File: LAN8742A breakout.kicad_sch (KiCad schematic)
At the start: 35 parts, among them J1 HR911105A_C12074, J2 J_RMII, J3 J_POW, SW1 nRST_SW, U1 LAN8720A, Y1 25MHz

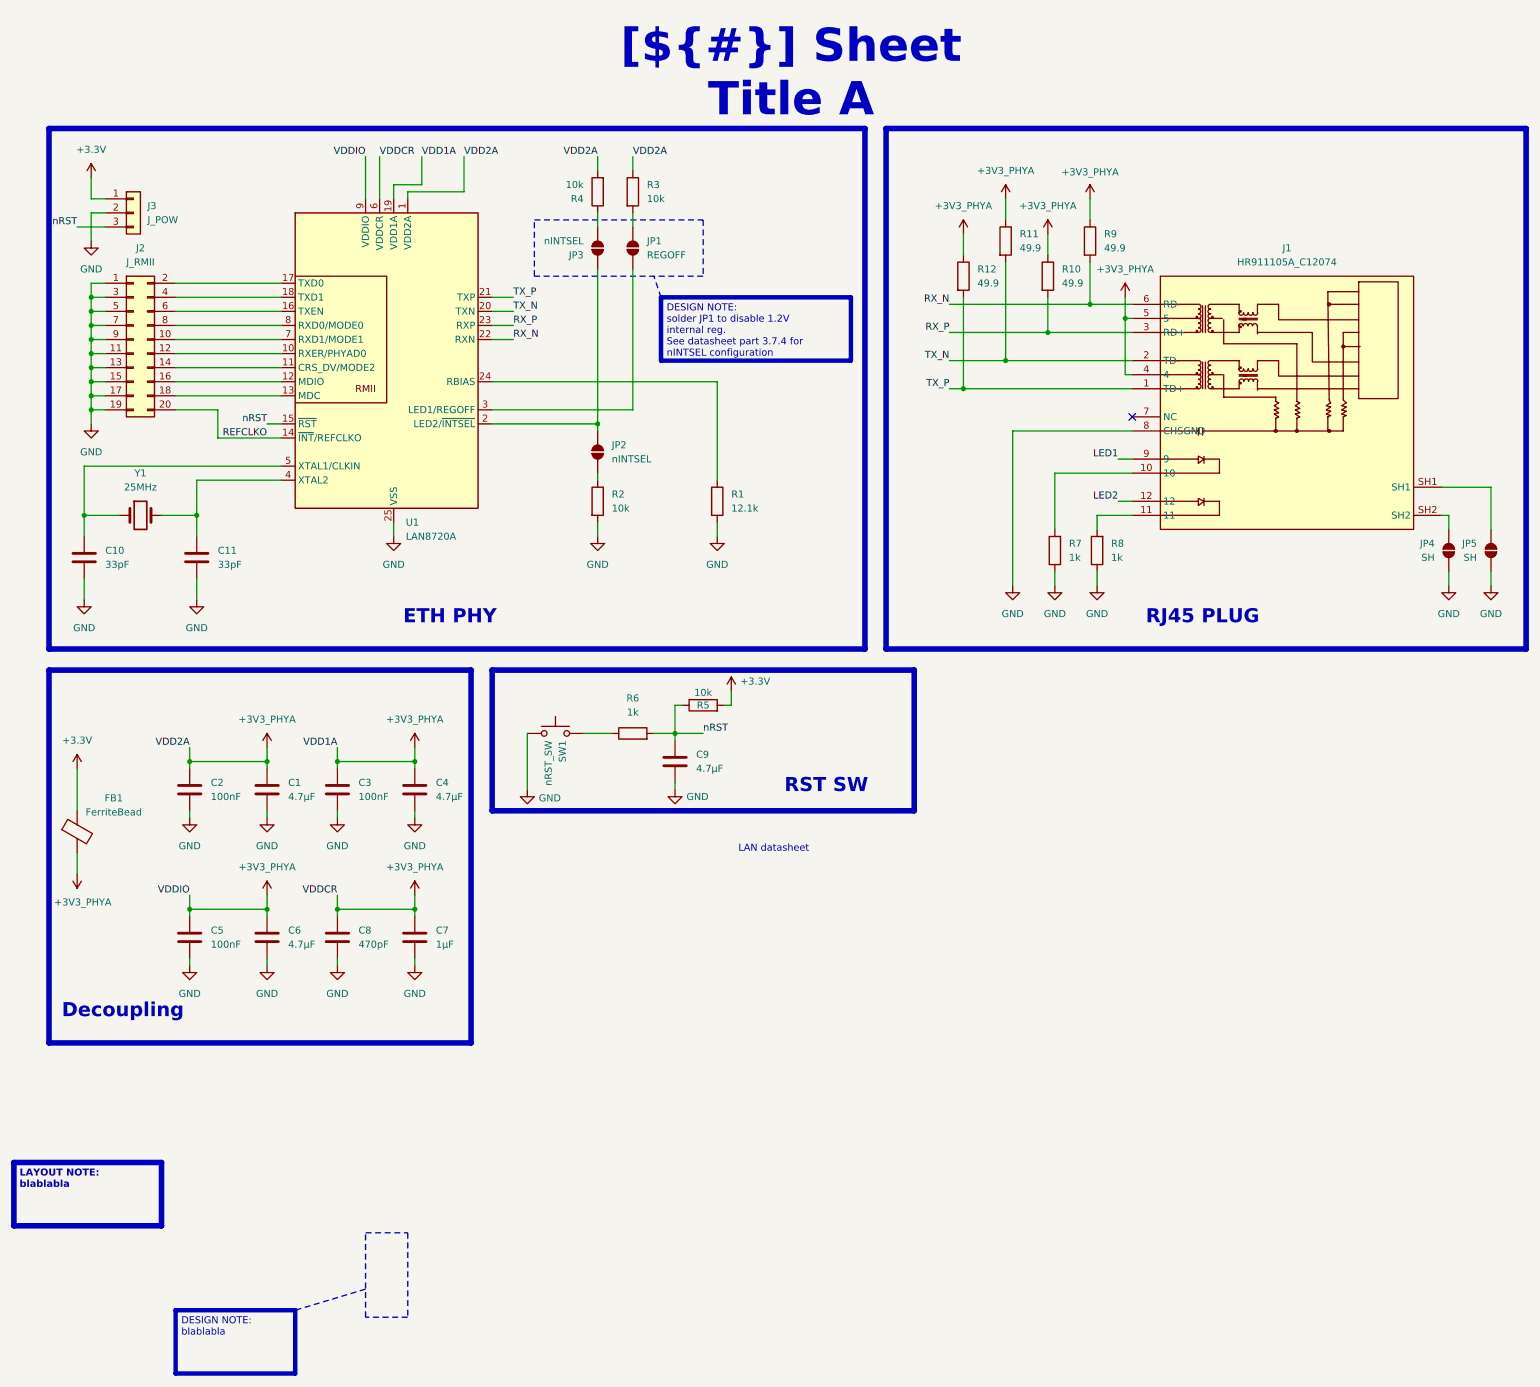
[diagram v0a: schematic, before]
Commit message: routed signals
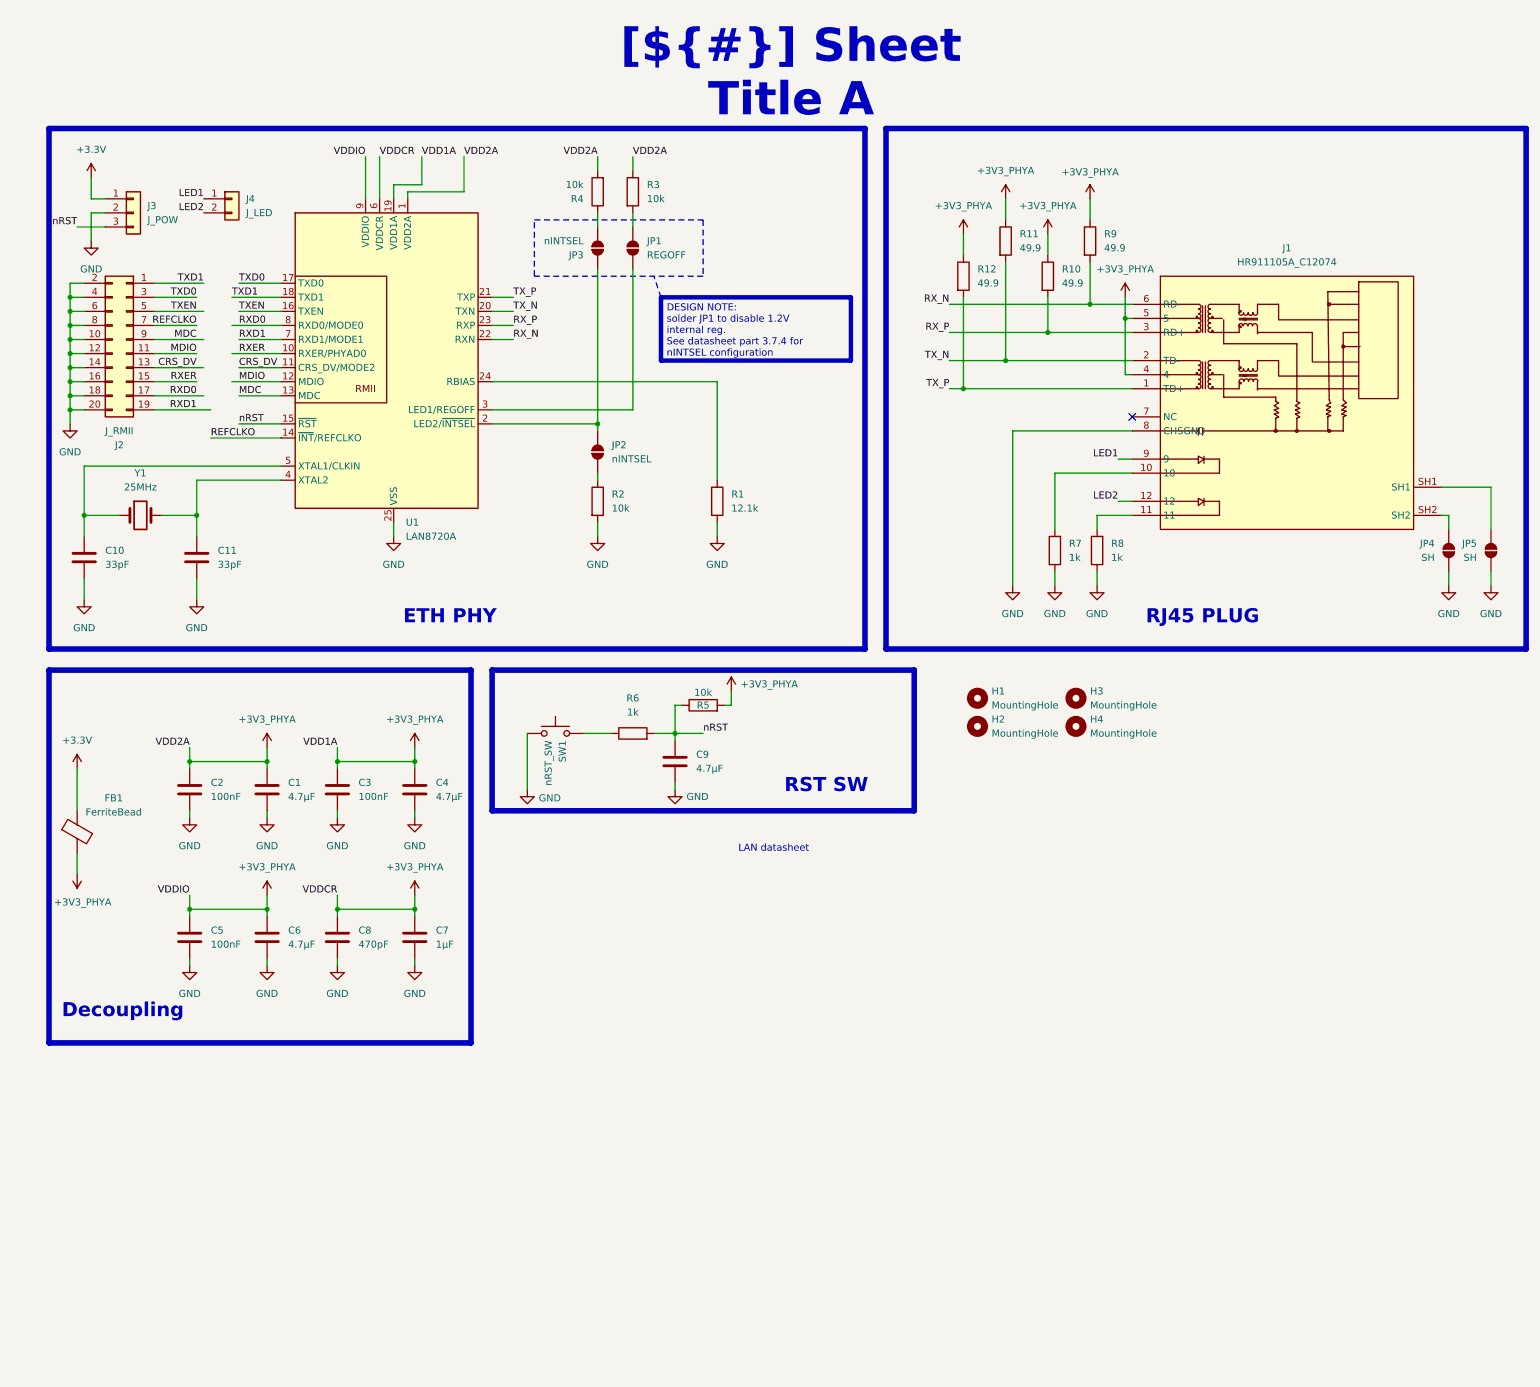
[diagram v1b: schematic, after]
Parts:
- added H1, H2, H3, H4: MountingHole, MountingHole:MountingHole_3.2mm_M3_DIN965, symbol Mechanical:MountingHole
- added J4: J_LED, Connector_PinSocket_2.54mm:PinSocket_1x02_P2.54mm_Vertical, symbol Connector_Generic:Conn_01x02
- FB1: footprint (none) -> 0_oscillators:L0603
- J2: footprint Connector_PinHeader_2.54mm:PinHeader_2x10_P2.54mm_Horizontal -> Connector_PinHeader_2.54mm:PinHeader_2x10_P2.54mm_Vertical
- SW1: footprint (none) -> Button_Switch_THT:SW_PUSH_6mm
- Y1: footprint (none) -> 0_oscillators:01.X.SD.120MMOI025000000
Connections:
- net +3.3V: no longer R5.2
- net +3V3_PHYA: now also R5.2
- net GND: now also J2.10 (Pin_10), J2.12 (Pin_12), J2.14 (Pin_14), J2.16 (Pin_16), J2.18 (Pin_18), J2.2 (Pin_2), J2.20 (Pin_20), J2.4 (Pin_4), J2.6 (Pin_6), J2.8 (Pin_8); no longer J2.1 (Pin_1), J2.11 (Pin_11), J2.13 (Pin_13), J2.15 (Pin_15), J2.17 (Pin_17), J2.19 (Pin_19), J2.3 (Pin_3), J2.5 (Pin_5), J2.7 (Pin_7), J2.9 (Pin_9)
- net LED1: now also J4.1 (Pin_1)
- net LED2: now also J4.2 (Pin_2)
- net REFCLKO: now also J2.7 (Pin_7); no longer J2.20 (Pin_20)
- net RXER: now reaches U1.10 (RXER/PHYAD0)
- net RXER: now also J2.15 (Pin_15); no longer J2.12 (Pin_12)
- net CRS_DV: now reaches U1.11 (CRS_DV/MODE2)
- net CRS_DV: now also J2.13 (Pin_13); no longer J2.14 (Pin_14)
- net MDIO: now reaches U1.12 (MDIO)
- net MDIO: now also J2.11 (Pin_11); no longer J2.16 (Pin_16)
- net MDC: now reaches U1.13 (MDC)
- net MDC: now also J2.9 (Pin_9); no longer J2.18 (Pin_18)
- net TXEN: now reaches U1.16 (TXEN)
- net TXEN: now also J2.5 (Pin_5); no longer J2.6 (Pin_6)
- net TXD0: now reaches U1.17 (TXD0)
- net TXD0: now also J2.3 (Pin_3); no longer J2.2 (Pin_2)
- net TXD1: now reaches U1.18 (TXD1)
- net TXD1: now also J2.1 (Pin_1); no longer J2.4 (Pin_4)
- net RXD1: now reaches U1.7 (RXD1/MODE1)
- net RXD1: now also J2.19 (Pin_19); no longer J2.10 (Pin_10)
- net RXD0: now reaches U1.8 (RXD0/MODE0)
- net RXD0: now also J2.17 (Pin_17); no longer J2.8 (Pin_8)
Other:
- moved on the sheet: J2

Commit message: finished routing & added silkscreen
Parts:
- J4: footprint Connector_PinSocket_2.54mm:PinSocket_1x02_P2.54mm_Vertical -> Connector_PinHeader_2.54mm:PinHeader_1x02_P2.54mm_Vertical
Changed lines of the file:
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@@
 			)
 		)
-		(property "Footprint" "Connector_PinSocket_2.54mm:PinSocket_1x02_P2.54mm_Vertical"
+		(property "Footprint" "Connector_PinHeader_2.54mm:PinHeader_1x02_P2.54mm_Vertical"
 			(at 50.8 44.45 0)
 			(effects

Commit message: stitching vias
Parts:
- J1: LCSC (none) -> C12074; LCSC Part C12074 -> (none)
- U1: LCSC (none) -> C510876

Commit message: jsp
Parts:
- J2, J3, J4, SW1: now left out of the parts list
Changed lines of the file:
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@@
 		(unit 1)
 		(exclude_from_sim no)
-		(in_bom yes)
+		(in_bom no)
 		(on_board yes)
 		(dnp no)
@@
 		(unit 1)
 		(exclude_from_sim no)
-		(in_bom yes)
+		(in_bom no)
 		(on_board yes)
 		(dnp no)
@@
 		(unit 1)
 		(exclude_from_sim no)
-		(in_bom yes)
+		(in_bom no)
 		(on_board yes)
 		(dnp no)
@@
 		(unit 1)
 		(exclude_from_sim no)
-		(in_bom yes)
-		(on_board yes)
-		(dnp no)
+		(in_bom no)
+		(on_board yes)
+		(dnp no)
